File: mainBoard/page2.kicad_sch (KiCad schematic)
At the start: 28 parts, among them IC1 TCAN3414DR, J10 RJ45, J11 RJ45, J12 Conn_02x20_Odd_Even, J13 RJ45, J14 RJ45, J15 RJ45, J16 BM04B-SRSS-TB, J17 BM04B-SRSS-TB, J18 BM04B-SRSS-TB, J19 BM04B-SRSS-TB, J20 BM04B-SRSS-TB, J7 RJ45, J8 RJ45, J9 RJ45, U3 TCA9548APWR

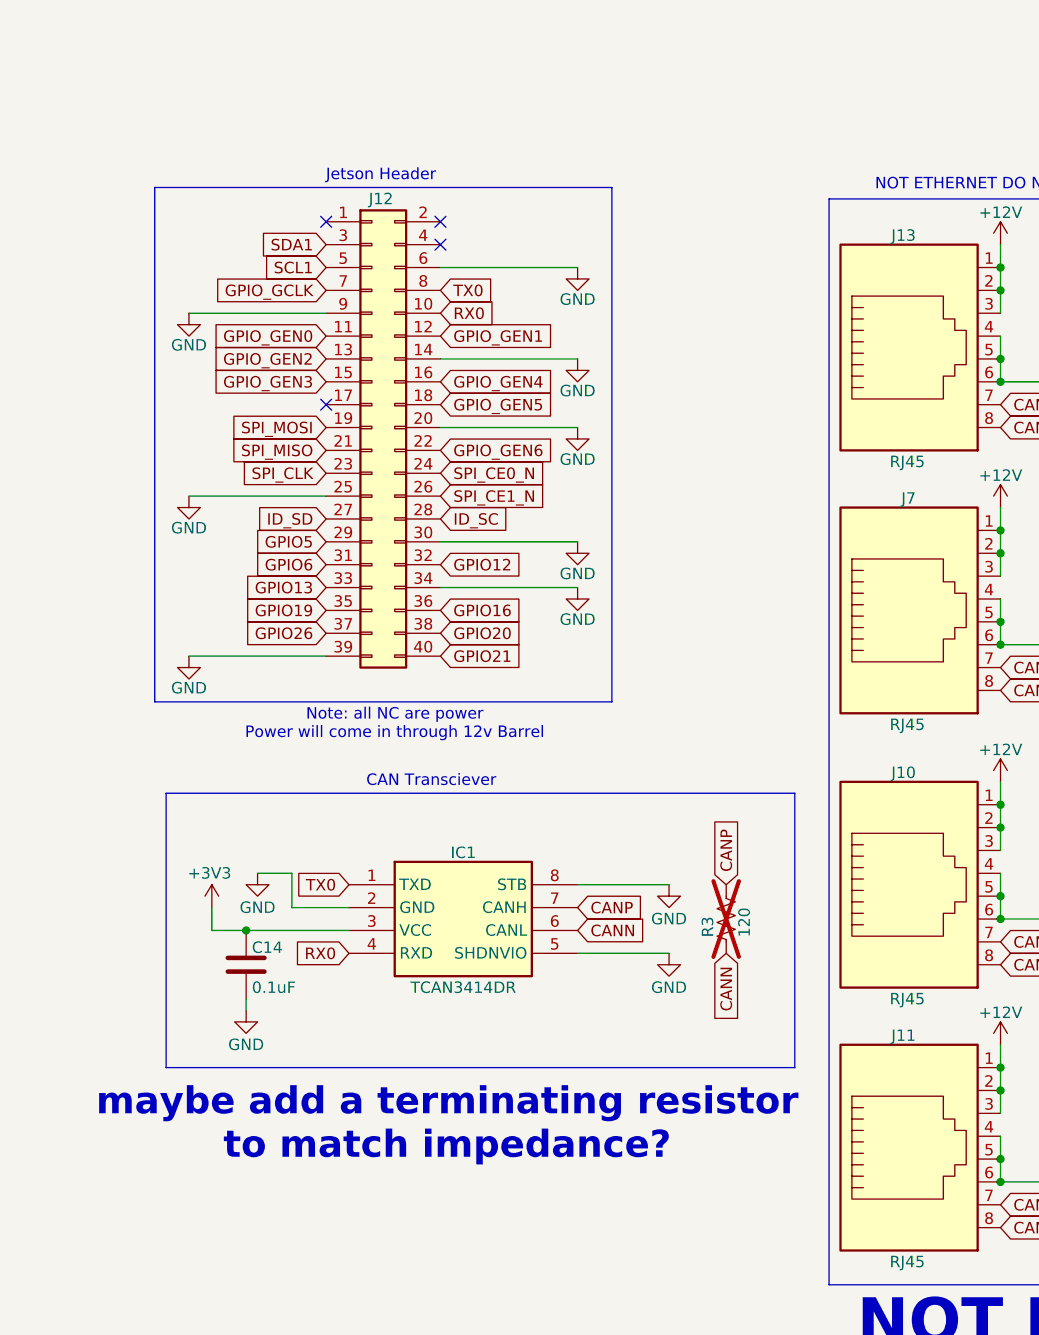
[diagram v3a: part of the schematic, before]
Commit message: Changed connector for jetson, adjusted layout, used vertical ethernet
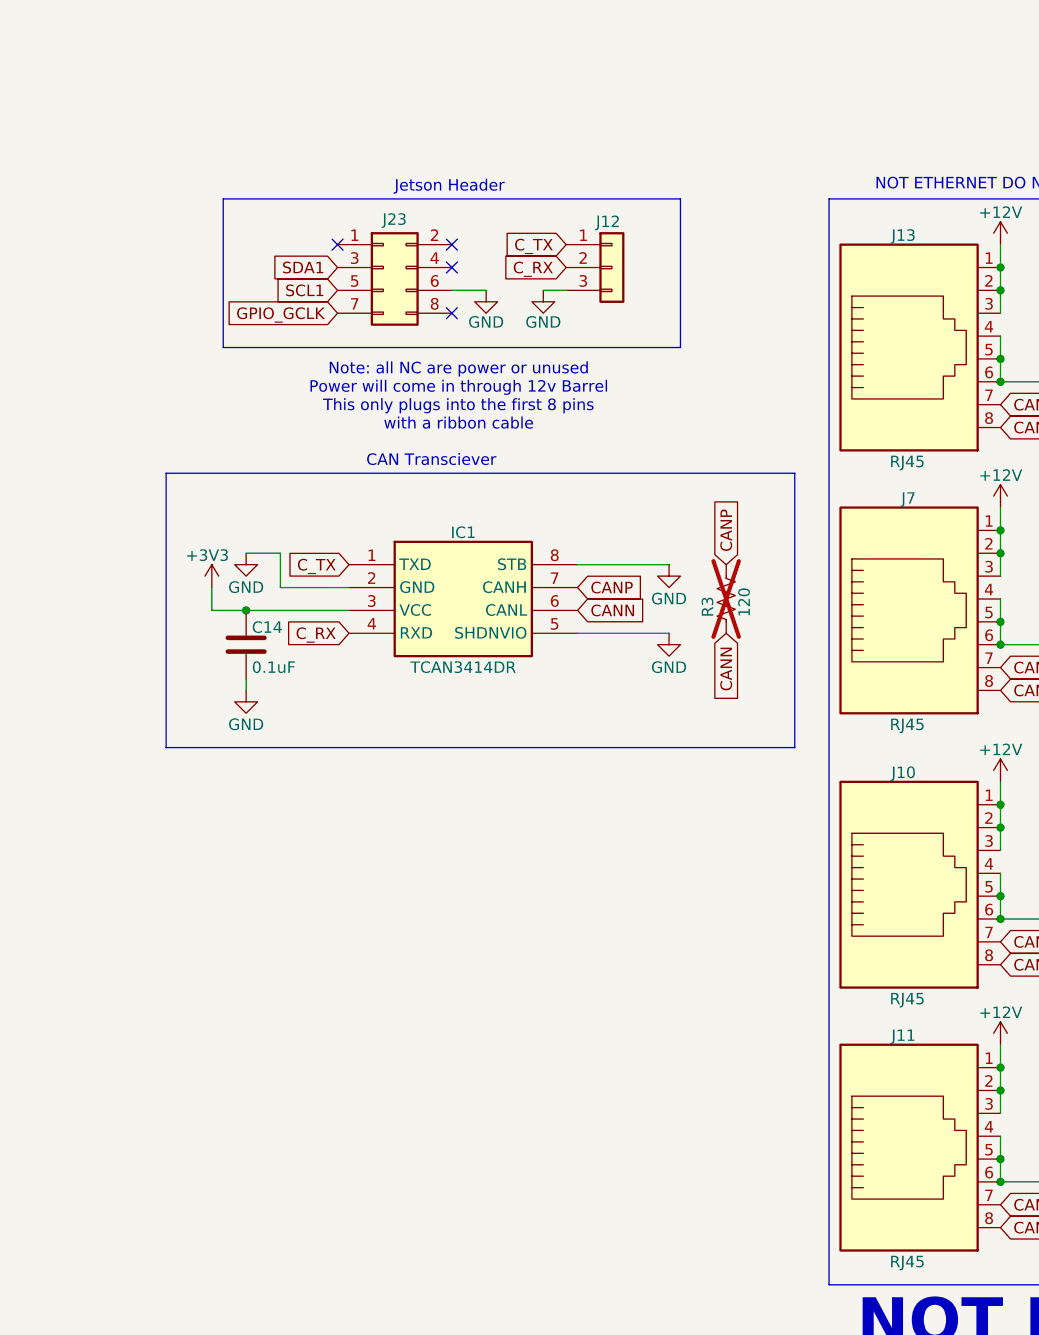
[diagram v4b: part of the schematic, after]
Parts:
- removed J12: Conn_02x20_Odd_Even, Connector_PinHeader_2.54mm:PinHeader_2x20_P2.54mm_Vertical, symbol Connector_Generic:Conn_02x20_Odd_Even
- added J12: Conn_01x03, Connector_PinHeader_2.54mm:PinHeader_1x03_P2.54mm_Vertical, symbol Connector_Generic:Conn_01x03
- added J23: Conn_02x04_Odd_Even, Connector_PinHeader_2.54mm:PinHeader_2x04_P2.54mm_Vertical, symbol Connector_Generic:Conn_02x04_Odd_Even
- J10, J11, J13, J14, J15, J7, J8, J9: footprint Connector_RJ:RJ45_Amphenol_54602-x08_Horizontal -> Connector_RJ:RJ45_OST_PJ012-8P8CX_Vertical
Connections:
- net GND: now also J12.3 (Pin_3), J23.6 (Pin_6)
- net GPIO_GCLK: now also J23.7 (Pin_7)
- net SCL1: now also J23.5 (Pin_5)
- net SDA1: now also J23.3 (Pin_3)
- net RX0 renamed C_RX
- net C_RX: now also J12.2 (Pin_2)
- net TX0 renamed C_TX
- net C_TX: now also J12.1 (Pin_1)
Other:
- note added: "Note: all NC are power or unused Power will come in through 12v Barrel This only plugs into the first 8 pins with a ribbon cable"
- note removed: "Note: all NC are power Power will come in through 12v Barrel"
- note removed: "maybe add a terminating resistor to match impedance?"
- moved on the sheet: C14, IC1, R3

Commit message: did some rearangement, added 3d models that were missing
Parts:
- added C16: 270pF, Capacitor_SMD:C_0805_2012Metric_Pad1.18x1.45mm_HandSolder, symbol Device:C
- added R24: 60, Resistor_SMD:R_0805_2012Metric_Pad1.20x1.40mm_HandSolder, symbol Device:R_US
- IC1: footprint footprints:SOIC127P600X175-8N -> Package_SO:SOIC-8_3.9x4.9mm_P1.27mm
- R3: value 120 -> 60
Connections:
- net GPIO21 is gone; now on net GPIO_GCLK: R23.2, U3.3 (~{RESET})
- net CANN: now also R24.2; no longer R3.2
- net GND: now also C16.2
- new net: C16.1, R24.1, R3.2
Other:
- note added: "Jetson Headers"
- note added: "Look more into this"
- note removed: "Jetson Header"
- moved on the sheet: C14, IC1, R3

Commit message: Updated schematic sheet to have proper name, date, orgnization, and note
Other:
- note removed: "1.1"
- note removed: "Main Board"
- note removed: "Summer 2024"
- company: (none) -> GRR
- title: (none) -> Main Board 2024
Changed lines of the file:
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@@
 	(generator_version "8.0")
 	(paper "A4")
+	(title_block
+		(title "Main Board 2024")
+		(rev "1.1")
+		(company "GRR")
+		(comment 1 "Currently WIP")
+	)
 	(junction
 		(at 186.69 77.47)
@@
 		)
 	)
-	(text "Main Board"
-		(exclude_from_sim no)
-		(at 191.77 189.738 0)
-		(effects
-			(font
-				(size 1.27 1.27)
-			)
-		)
-	)
 	(text "CAN Transciever"
 		(exclude_from_sim no)
@@
 			)
 		)
-	)
-	(text "Summer 2024"
-		(exclude_from_sim no)
-		(at 212.598 193.548 0)
-		(effects
-			(font
-				(size 1.27 1.27)
-			)
-		)
-	)
-	(text "1.1"
-		(exclude_from_sim no)
-		(at 269.494 193.548 0)
-		(effects
-			(font
-				(size 1.27 1.27)
-			)
-		)

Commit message: more notes
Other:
- note added: "Look more into this capacitor value 1/2πrc"
- note removed: "Look more into this"
- title: Main Board 2024 -> Main Board 2024-2025
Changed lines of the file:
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@@
 	(paper "A4")
 	(title_block
-		(title "Main Board 2024")
+		(title "Main Board 2024-2025")
 		(rev "1.1")
 		(company "GRR")
 		(comment 1 "Currently WIP")
+		(comment 2 "Please check CAN capacitor value")
 	)
 	(junction
@@
 		)
 	)
-	(text "Look more into this"
+	(text "Look more into this\ncapacitor value\n1/2πrc"
 		(exclude_from_sim no)
-		(at 71.628 101.092 0)
+		(at 72.39 104.902 0)
 		(effects
 			(font

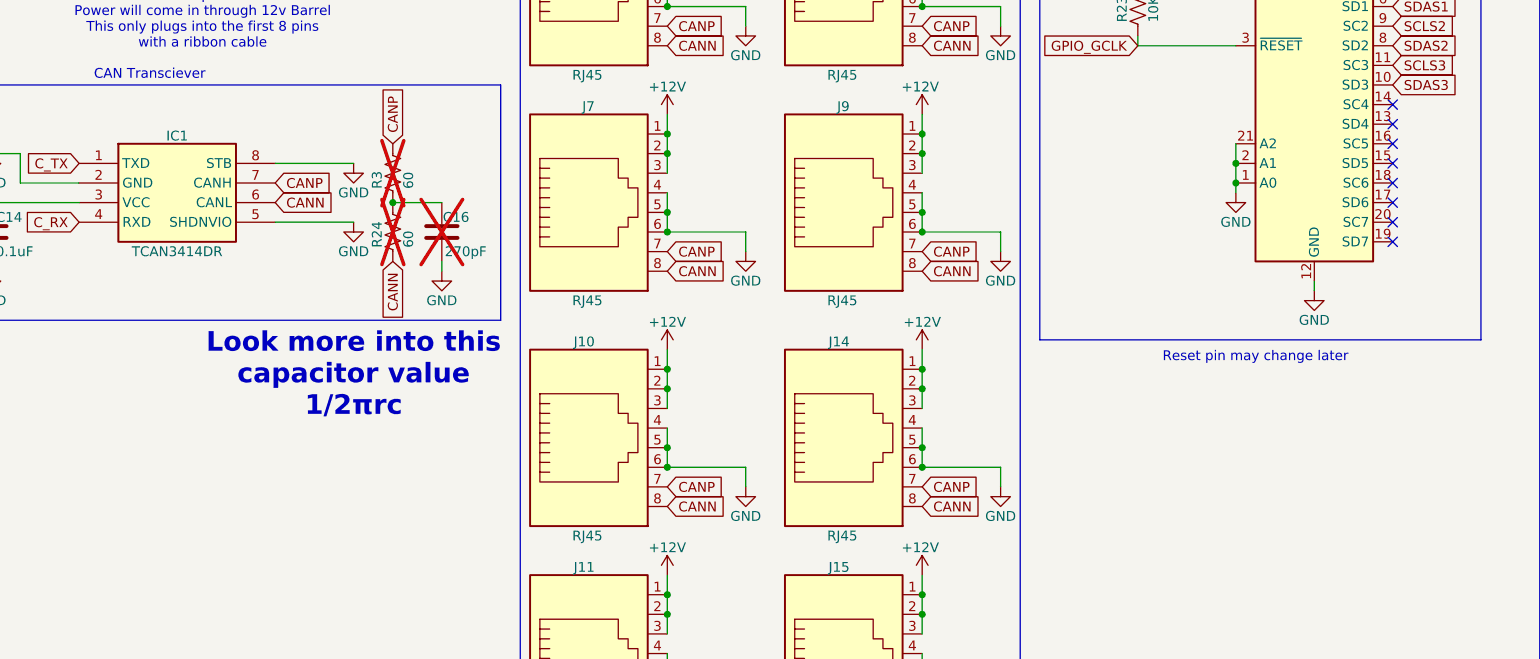
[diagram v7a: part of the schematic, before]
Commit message: updated capacitor value for can split termination
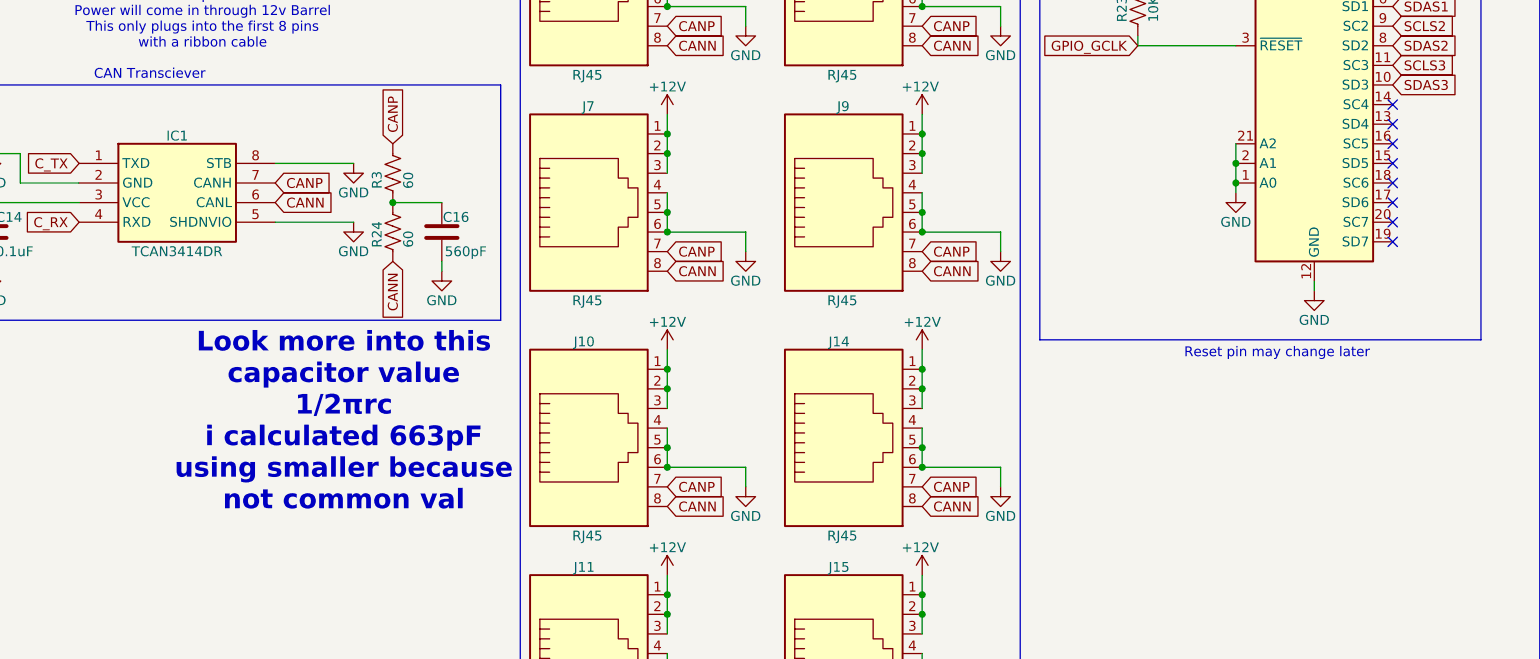
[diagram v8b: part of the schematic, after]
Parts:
- C16: value 270pF -> 560pF; now fitted
- R24, R3: now fitted
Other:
- note added: "Look more into this capacitor value 1/2πrc i calculated 663pF using smaller because not common val"
- note removed: "Look more into this capacitor value 1/2πrc"
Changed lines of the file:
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@@
 		)
 	)
-	(text "Look more into this\ncapacitor value\n1/2πrc"
+	(text "Look more into this\ncapacitor value\n1/2πrc\ni calculated 663pF\nusing smaller because\nnot common val"
 		(exclude_from_sim no)
-		(at 72.39 104.902 0)
+		(at 71.12 110.998 0)
 		(effects
 			(font
@@
 	(text "Reset pin may change later"
 		(exclude_from_sim no)
-		(at 189.23 102.616 0)
+		(at 192.024 102.108 0)
 		(effects
 			(font
@@
 		(in_bom yes)
 		(on_board yes)
-		(dnp yes)
+		(dnp no)
 		(property "Reference" "C16"
 			(at 83.947 84.4549 0)
@@
 			)
 		)
-		(property "Value" "270pF"
+		(property "Value" "560pF"
 			(at 84.201 88.8999 0)
 			(effects
@@
 		(in_bom yes)
 		(on_board yes)
-		(dnp yes)
+		(dnp no)
 		(property "Reference" "R3"
 			(at 75.438 80.7719 90)
@@
 		(in_bom yes)
 		(on_board yes)
-		(dnp yes)
+		(dnp no)
 		(property "Reference" "R24"
 			(at 75.438 88.3919 90)
